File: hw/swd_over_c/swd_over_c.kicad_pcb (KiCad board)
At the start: 4 copper layers, 20.5 x 11 mm, 23 parts, among them J1 USB_C_Receptacle_USB2.0, J2 Conn_ARM_JTAG_SWD_10, P1 USB_C_Plug, U1 ATtiny24-20M

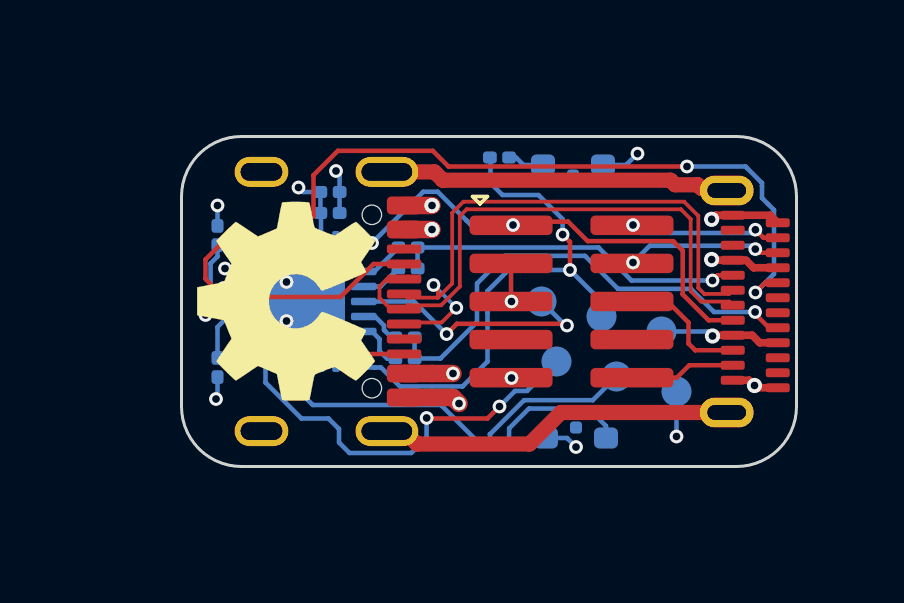
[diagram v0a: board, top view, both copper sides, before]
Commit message: Updated swd over c to v1.1 (and programmer)
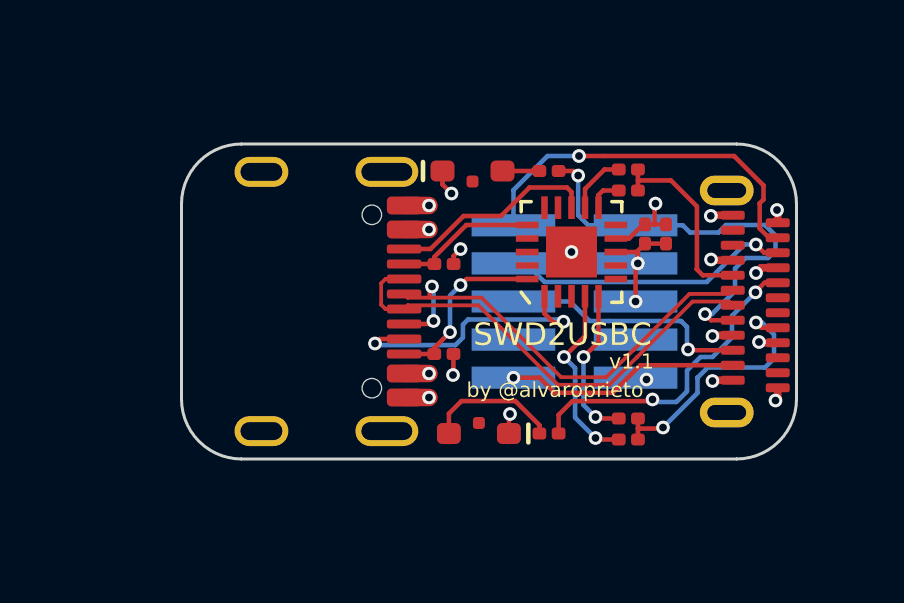
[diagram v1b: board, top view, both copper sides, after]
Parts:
- removed TP1: VBUS, alvarop:TP-1mm
- removed TP2: GND, alvarop:TP-1mm
- removed TP3: SCK, alvarop:TP-1mm
- removed TP4: MISO, alvarop:TP-1mm
- removed TP5: MOSI, alvarop:TP-1mm
- removed TP6: NRST, alvarop:TP-1mm
- C1, C2, D1, D2, R1, R2, R3, R4, R5, R6, R7, R8: moved to F.Cu
- J2: footprint alvarop:3220-10-0300-00 -> snapeda:SAMTEC_FTSH-105-01-F-DV-P-TR; moved to B.Cu
- REF**: moved to B.Cu
- U1: footprint Package_DFN_QFN:QFN-20-1EP_4x4mm_P0.5mm_EP2.6x2.6mm -> ultralibrarian:ATTINY24A-MMH; moved to F.Cu
- moved C2 11.2 mm to (175.2, 65.2), turned to -90 degrees
- moved C1 10.6 mm to (174.4, 65.2), turned to -90 degrees
- moved D1 9.55 mm to (168.7, 63.1)
- moved D2 9.48 mm to (168.9, 71.9)
- moved R8 9.35 mm to (171.2, 71.9), turned to 0 degrees
- moved R7 9.25 mm to (171.2, 63.1), turned to 180 degrees
- moved U1 9.00 mm to (172.0, 65.8), turned to 90 degrees
- moved R5 8.18 mm to (173.9, 72.1)
- moved R4 8.05 mm to (173.9, 63.1)
- moved R6 7.71 mm to (173.9, 71.4)
- moved R2 7.61 mm to (167.8, 66.2), turned to 180 degrees
- moved R3 7.59 mm to (173.9, 63.8)
- moved R1 7.56 mm to (167.7, 69.2), turned to 180 degrees
- moved REF** 0.30 mm to (162.8, 67.5)
- moved J2 0.10 mm to (172.1, 67.5)
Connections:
- J1 pad A5: /CC1_IN -> /CC1_IN_MOSI
- J1 pad A8: unconnected-(J1-PadA8) -> /SCK
- J1 pad B5: /CC2_IN -> /CC2_IN_MISO
- J1 pad B8: unconnected-(J1-PadB8) -> /MCURST
- R1 pad 2: /CC2_IN -> /CC2_IN_MISO
- R2 pad 2: /CC1_IN -> /CC1_IN_MOSI
- R7 pad 1: /MISO -> /SBU1
- R8 pad 2: /MOSI -> /SBU2
- U1 pad 14: /CC2_R1 -> unconnected-(U1-Pad14)
- U1 pad 15: /CC2_R2 -> unconnected-(U1-Pad15)
- U1 pad 16: /MOSI -> /CC1_IN_MOSI
- U1 pad 2: /CC2_IN -> unconnected-(U1-Pad2)
- U1 pad 20: /MISO -> /CC2_IN_MISO
- U1 pad 3: /CC1_IN -> unconnected-(U1-Pad3)
- U1 pad 4: /SBU2 -> /CC2_R1
- U1 pad 5: /SBU1 -> /CC2_R2
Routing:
- net /SHIELD: track 23.5 -> 43.2 mm
- net /MOSI: track 18.7 -> 0.00 mm, vias 2 -> 0
- net /SBU2: track 28.5 -> 10.7 mm, vias 3 -> 2
- net /MISO: track 13.8 -> 0.00 mm
- net /CC1_IN: track 11.0 -> 0.00 mm, vias 1 -> 0
- net /CC2_IN: track 8.47 -> 0.00 mm, vias 1 -> 0
- net /SWDIO: track 5.13 -> 12.6 mm, vias 2 -> 1
- net /SBU1: track 21.6 -> 14.3 mm, vias 3 -> 2
- net /CC2: track 16.0 -> 8.86 mm, vias 1 -> 2
- net /CC2_IN_MISO: track 0.00 -> 5.97 mm, vias 0 -> 2
- net GND: track 16.3 -> 10.7 mm, vias 17 -> 14
- net /CC1: track 11.7 -> 6.40 mm, vias 1 -> 0
- net /SCK: track 14.5 -> 9.32 mm
- net /CC2_R1: track 1.43 -> 6.24 mm, vias 0 -> 2
- net /CC1_IN_MOSI: track 0.00 -> 4.78 mm
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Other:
- board size 20.5 x 11 mm -> 20.5 x 10.5 mm
- board text added: "SWD2USBC"
- board text added: "v1.1"
- board text removed: "GND"
- board text removed: "MISO"
- board text removed: "MOSI"
- board text removed: "RST"
- board text removed: "SCK"
- board text removed: "SWD to USB-C"
- board text removed: "VBUS"
- board text removed: "v1.0"

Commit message: Switched to 0402 instead of 0201 components
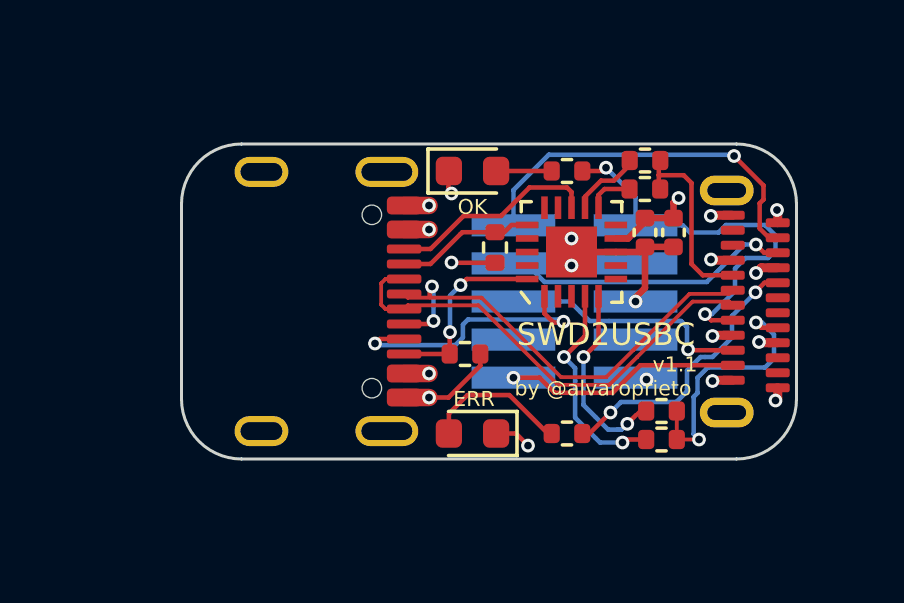
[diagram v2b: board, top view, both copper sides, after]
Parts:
- C1, C2: footprint Capacitor_SMD:C_0201_0603Metric -> Capacitor_SMD:C_0402_1005Metric
- D1, D2: footprint alvarop:HSMx-C120 -> LED_SMD:LED_0603_1608Metric
- R1, R2, R3, R4, R5, R6, R7, R8: footprint Resistor_SMD:R_0201_0603Metric -> Resistor_SMD:R_0402_1005Metric
- moved R2 1.79 mm to (169.4, 65.7), turned to 90 degrees
- moved R6 1.13 mm to (175.0, 71.2)
- moved R5 1.10 mm to (175.0, 72.1)
- moved R1 0.70 mm to (168.4, 69.2)
- moved R4 0.63 mm to (174.4, 62.8)
- moved R7 0.60 mm to (171.8, 63.1)
- moved R8 0.60 mm to (171.8, 71.9)
- moved R3 0.55 mm to (174.4, 63.8)
- moved C2 0.25 mm to (175.4, 65.2)
- moved D2 0.21 mm to (168.7, 71.9), turned to 180 degrees
- turned D1 to 0 degrees
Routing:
- net GND: track 10.7 -> 18.0 mm, vias 14 -> 13
- net /SHIELD: track 43.2 -> 41.4 mm
- net /CC2_R2: track 5.19 -> 6.52 mm
- net /SBU2: track 10.7 -> 9.44 mm
- net /CC2_R1: track 6.24 -> 7.24 mm
- net /SBU1: track 14.3 -> 13.4 mm
- net VBUS: track 7.05 -> 7.69 mm
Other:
- board text added: "ERR"
- board text added: "OK"

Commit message: SWD2USBC v1.2
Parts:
- moved REF** 4.30 mm to (158.5, 67.5)
- moved R1 4.03 mm to (164.4, 69.5), turned to 90 degrees
- moved J1 3.80 mm to (162.6, 67.5)
- moved C1 3.50 mm to (170.9, 65.2)
- moved C2 3.50 mm to (171.9, 65.2)
- moved D1 3.50 mm to (165.2, 63.1)
- moved J2 3.50 mm to (168.6, 67.5)
- moved R2 3.50 mm to (165.9, 65.7)
- moved R3 3.50 mm to (170.9, 63.8)
- moved R4 3.50 mm to (170.9, 62.8)
- moved R7 3.50 mm to (168.3, 63.1)
- moved U1 3.50 mm to (168.5, 65.8)
- moved D2 3.45 mm to (165.2, 71.9)
- moved R5 3.45 mm to (171.6, 72.1)
- moved R6 3.45 mm to (171.6, 71.2)
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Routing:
- net /SHIELD: track 41.4 -> 52.0 mm
- net /SWDCLK: track 9.70 -> 15.1 mm
- net /D+: track 15.9 -> 20.3 mm
- net /D-: track 15.7 -> 20.0 mm
- net /CC2: track 9.05 -> 13.3 mm
- net /NRST: track 7.90 -> 11.8 mm
- net /CC1: track 6.37 -> 9.86 mm
- net /SBU2: track 9.44 -> 12.6 mm
- net /SWO: track 8.40 -> 11.5 mm
- net /SWDIO: track 12.6 -> 14.6 mm
- net GND: track 18.0 -> 19.4 mm, vias 13 -> 14
- net /SBU1: track 13.4 -> 12.1 mm
- net /SCK: track 9.32 -> 10.3 mm
- net VBUS: track 7.69 -> 6.80 mm
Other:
- board size 20.5 x 10.5 mm -> 24.2 x 16 mm
- board text added: "v1.2"
- board text removed: "v1.1"

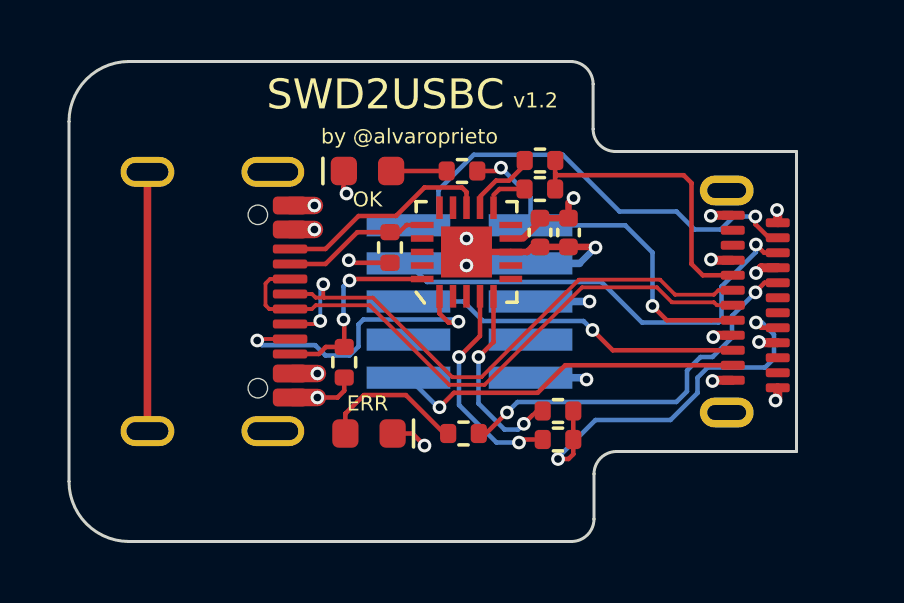
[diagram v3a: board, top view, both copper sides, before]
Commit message: Fixed MISO/MOSI swap and added BOM to swd2usbc
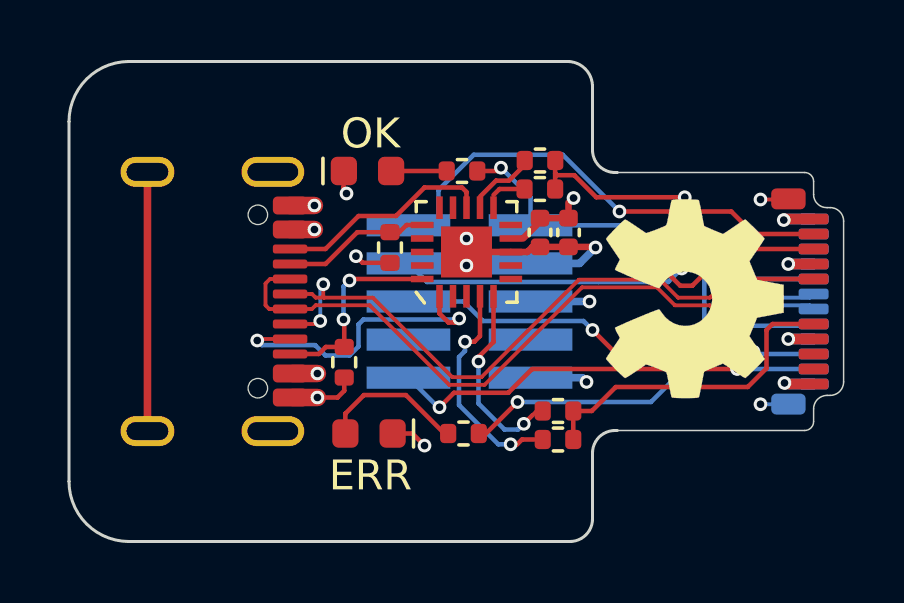
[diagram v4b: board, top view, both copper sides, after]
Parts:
- P1: footprint alvarop:‎USB4155-03-C‎ -> alvarop:MOLEX_1054440011; moved to B.Cu
- REF**: moved to F.Cu
- moved REF** 17.6 mm to (176.1, 67.4), turned to -90 degrees
- moved P1 0.59 mm to (180.1, 67.5)
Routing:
- net /SHIELD: track 52.0 -> 57.0 mm, vias 0 -> 2
- net /SBU1: track 12.1 -> 15.5 mm, vias 2 -> 3
- net /D-: track 20.0 -> 22.9 mm, vias 0 -> 1
- net /D+: track 20.3 -> 23.2 mm, vias 2 -> 3
- net /SWO: track 11.5 -> 14.2 mm, vias 1 -> 2
- net /NRST: track 11.8 -> 14.4 mm, vias 1 -> 2
- net /CC2: track 13.3 -> 10.9 mm, vias 2 -> 0
- net /SBU2: track 12.6 -> 14.4 mm
- net /CC1: track 9.86 -> 11.6 mm, vias 0 -> 1
- net GND: track 19.4 -> 20.9 mm, vias 14 -> 12
- net /SWDCLK: track 15.1 -> 14.2 mm
- net /SWDIO: track 14.6 -> 15.3 mm
- net VBUS: track 6.80 -> 7.30 mm, vias 7 -> 5
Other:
- board size 24.2 x 16 mm -> 18.3 x 16 mm
- board text added: "v1.3"
- board text removed: "v1.2"

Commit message: SWD over USB-C v1.4!!!
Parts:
- J1: value USB_C_Receptacle_USB2.0 -> USB-C Receptacle; footprint alvarop:USB4105-GF-A -> alvarop:USB4500-03
- P1: moved to F.Cu
- R3: value 10k -> 22k
- R4: value 22k -> 56k
- R5: value 22k -> 10k
- R6: value 56k -> 22k
- REF**: moved to B.Cu
- U1: footprint ultralibrarian:ATTINY24A-MMH -> ultralibrarian:ATTINY24A-MMH_MOD
- moved J1 1.42 mm to (161.2, 67.5)
- moved R5 1.25 mm to (170.3, 72.1)
- moved R6 1.25 mm to (170.3, 71.2), turned to 0 degrees
- moved R1 0.93 mm to (165.3, 69.2)
- moved R8 0.60 mm to (167.8, 71.9)
- moved R7 0.55 mm to (167.8, 63.1)
- moved C1 0.42 mm to (170.9, 65.6)
- moved C2 0.42 mm to (171.9, 65.6)
- moved R3 0.35 mm to (170.7, 63.5), turned to 180 degrees
- moved R4 0.35 mm to (170.7, 62.5), turned to 180 degrees
- moved REF** 0.15 mm to (176.1, 67.5), turned to 90 degrees
- turned P1 to -90 degrees
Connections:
- R3 pad 1: /CC1_R1 -> /CC1
- R3 pad 2: /CC1 -> /CC1_R1
- R4 pad 1: /CC1_R2 -> /CC1
- R4 pad 2: /CC1 -> /CC1_R2
- R6 pad 1: /CC2 -> /CC2_R2
- R6 pad 2: /CC2_R2 -> /CC2
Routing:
- net /SHIELD: track 57.0 -> 19.5 mm, vias 2 -> 0
- net /CC2_IN_MISO: track 6.65 -> 10.1 mm
- net /D+: track 23.2 -> 26.0 mm, vias 3 -> 2
- net /SBU2: track 14.4 -> 16.4 mm, vias 2 -> 1
- net /CC2: track 10.9 -> 12.7 mm, vias 0 -> 1
- net /CC2_R2: track 6.54 -> 4.78 mm
- net /D-: track 22.9 -> 24.5 mm, vias 1 -> 2
- net /NRST: track 14.4 -> 15.7 mm, vias 2 -> 1
- net /CC2_R1: track 7.49 -> 6.25 mm
- net VBUS: track 7.30 -> 8.39 mm
- net /SWDIO: track 15.3 -> 14.3 mm, vias 1 -> 0
- net /SCK: track 10.4 -> 9.52 mm
- net /CC1_IN_MOSI: track 4.94 -> 5.81 mm
- net /MCURST: track 7.31 -> 8.18 mm
- net /SBU1: track 15.5 -> 16.3 mm, vias 3 -> 4
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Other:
- board size 18.3 x 16 mm -> 18.5 x 16 mm
- board text added: "Leave room for USB-C plug here!"
- board text added: "v1.4"
- board text removed: "v1.3"
